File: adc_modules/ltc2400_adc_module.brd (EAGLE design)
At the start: 100 x 80 mm, 0 parts

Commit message: * small modifications on ltc2400_adc_module
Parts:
- added C3: 10u, SquantorRCL:C0805
- added JP1, JP2: (no value), SquantorConnectors:1X10_NORMAL_OCT
- added R2: ferrite, SquantorRCL:R0805
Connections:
- new net GND: C3.1, JP1.2, JP1.3, JP1.6, JP2.1, JP2.2
- new net GND_ADC: JP2.9
- new net N$1: JP1.1, R2.1
- new net N$13: JP2.3
- new net N$14: JP2.4
- new net N$15: JP2.5
- new net N$16: JP2.6
- new net N$17: JP2.7
- new net N$18: JP2.8
- new net V+: JP1.7
- new net V-: JP1.10
- new net VCC_ADC: JP2.10
- new net VCC_VREF: C3.2, R2.2
- new net VIN+: JP1.8
- new net VIN-: JP1.9
- new net VREF_IN: JP1.4
- new net VREF_OUT: JP1.5

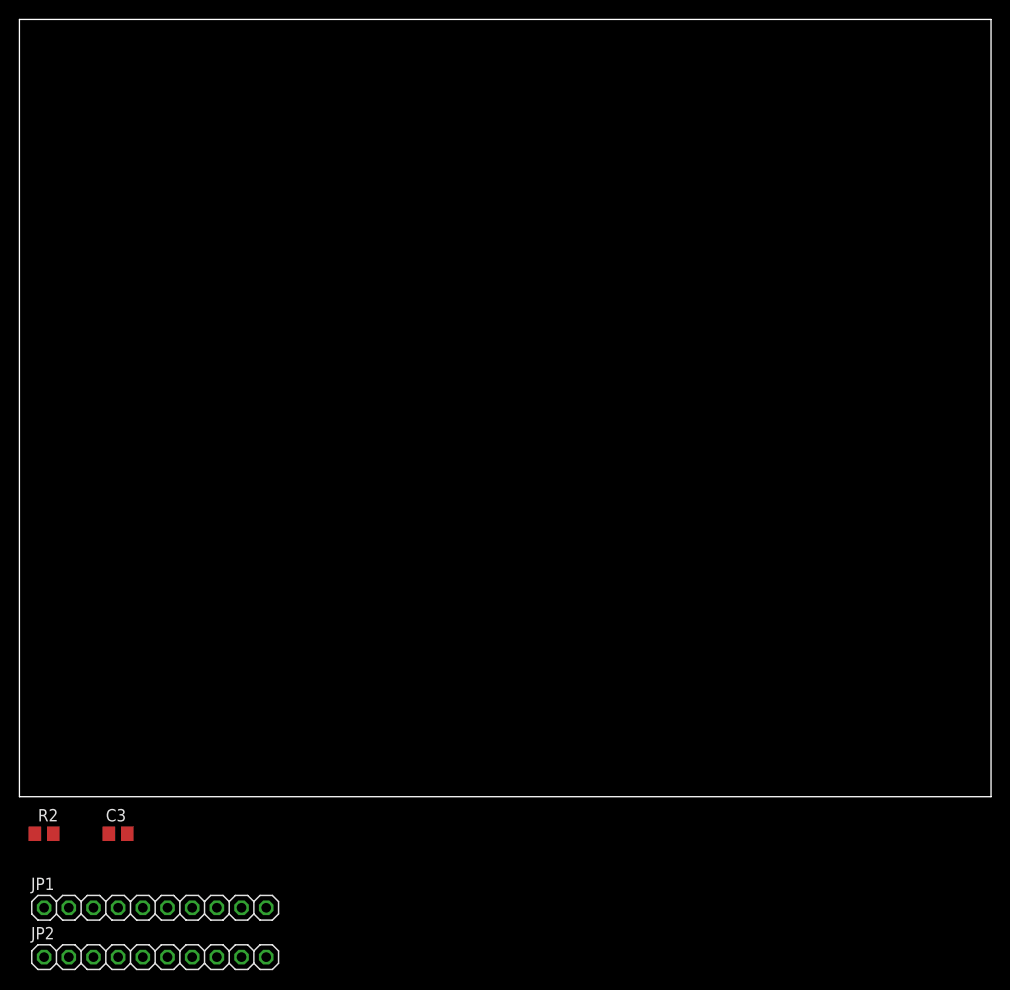
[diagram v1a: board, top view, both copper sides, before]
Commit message: * updated and almost finished MCP3551 ADC module
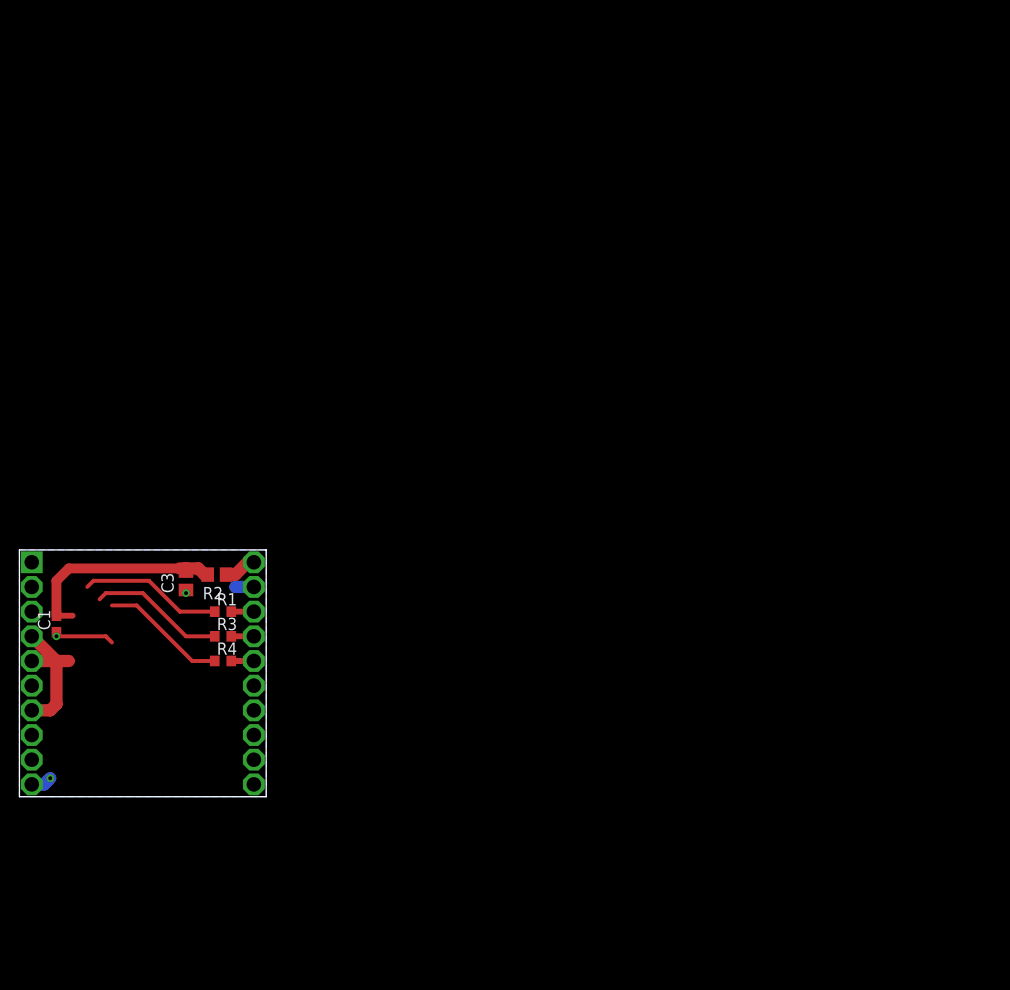
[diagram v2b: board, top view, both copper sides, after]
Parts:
- removed JP1, JP2: (no value), SquantorConnectors:1X10_NORMAL_OCT
- added C1: 100n, SquantorRCL:C0603
- added R1, R3, R4: 100, SquantorRCL:R0603
- added U$1: METROLOGY_MODULE1.5MM, SquantorPCBOutline:METROLOGY_MODULE_1.5MM_HOLE
- moved R2 32.1 mm to (20.3, 22.9), turned to 180 degrees
- moved C3 27.0 mm to (17.1, 22.2), turned to 90 degrees
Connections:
- removed net GND_ADC: JP2.9
- removed net N$13: JP2.3
- removed net N$14: JP2.4
- removed net N$15: JP2.5
- removed net N$16: JP2.6
- removed net N$17: JP2.7
- removed net N$18: JP2.8
- removed net V+: JP1.7
- removed net V-: JP1.10
- removed net VCC_ADC: JP2.10
- removed net VCC_VREF: C3.2, R2.2
- removed net VIN+: JP1.8
- removed net VIN-: JP1.9
- removed net VREF_IN: JP1.4
- removed net VREF_OUT: JP1.5
- new net ADC_CS: R1.1
- new net ADC_SCK: R4.1
- new net ADC_SDO: R3.1
- new net N$2: R1.2, U$1.P$18
- new net N$3: R3.2, U$1.P$17
- new net N$4: R4.2, U$1.P$16
- new net N$5: U$1.P$8
- new net N$6: U$1.P$9
- new net VCC: C1.2, C3.2, R2.2
- new net VREF: U$1.P$4, U$1.P$5, U$1.P$7
- net GND: now also C1.1, U$1.P$10, U$1.P$19, U$1.P$6; no longer JP1.2, JP1.3, JP1.6, JP2.1, JP2.2
- net N$1: now also U$1.P$20; no longer JP1.1
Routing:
- net VCC: track 0.00 -> 21.9 mm
- net VREF: track 0.00 -> 15.1 mm
- net ADC_CS: track 0.00 -> 14.7 mm
- net ADC_SDO: track 0.00 -> 14.0 mm
- net ADC_SCK: track 0.00 -> 12.9 mm
- net GND: track 0.00 -> 10.5 mm, vias 0 -> 3
- net N$1: track 0.00 -> 3.39 mm
- net N$4: track 0.00 -> 2.32 mm
- net N$3: track 0.00 -> 2.32 mm
- net N$2: track 0.00 -> 2.32 mm
- added copper zone on layer 16, net GND
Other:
- board size 100 x 80 mm -> 25.4 x 25.4 mm
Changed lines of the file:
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@@
 <setting verticaltext="up"/>
 </settings>
-<grid distance="2.54" unitdist="mm" unit="mm" style="lines" multiple="1" display="yes" altdistance="0.025" altunitdist="inch" altunit="inch"/>
+<grid distance="0.635" unitdist="mm" unit="mm" style="lines" multiple="1" display="yes" altdistance="0.025" altunitdist="inch" altunit="inch"/>
 <layers>
 <layer number="1" name="Top" color="4" fill="1" visible="yes" active="yes"/>
@@
 <board>
 <plain>
-<wire x1="0" y1="0" x2="100" y2="0" width="0" layer="20"/>
-<wire x1="100" y1="0" x2="100" y2="80" width="0" layer="20"/>
-<wire x1="100" y1="80" x2="0" y2="80" width="0" layer="20"/>
-<wire x1="0" y1="80" x2="0" y2="0" width="0" layer="20"/>
+<wire x1="0" y1="25.4" x2="25.4" y2="25.4" width="0" layer="20"/>
 </plain>
 <attributes>
@@
 </autorouter>
 <elements>
-<element name="JP1" library="SquantorConnectors" package="1X10_NORMAL_OCT" value="" x="13.97" y="-11.43"/>
-<element name="JP2" library="SquantorConnectors" package="1X10_NORMAL_OCT" value="" x="13.97" y="-16.51"/>
-<element name="R2" library="SquantorRCL" package="R0805" value="ferrite" x="2.54" y="-3.81"/>
-<element name="C3" library="SquantorRCL" package="C0805" value="10u" x="10.16" y="-3.81"/>
+<element name="R2" library="SquantorRCL" package="R0805" value="ferrite" x="20.32" y="22.86" rot="R180"/>
+<element name="C3" library="SquantorRCL" package="C0805" value="10u" x="17.145" y="22.225" rot="R90"/>
+<element name="U$1" library="SquantorPCBOutline" package="METROLOGY_MODULE_1.5MM_HOLE" value="METROLOGY_MODULE1.5MM" x="12.7" y="12.7"/>
+<element name="C1" library="SquantorRCL" package="C0603" value="100n" x="3.81" y="17.78" rot="R90"/>
+<element name="R1" library="SquantorRCL" package="R0603" value="100" x="20.955" y="19.05"/>
+<element name="R3" library="SquantorRCL" package="R0603" value="100" x="20.955" y="16.51"/>
+<element name="R4" library="SquantorRCL" package="R0603" value="100" x="20.955" y="13.97"/>
 </elements>
 <signals>
-<signal name="VCC_VREF">
+<signal name="VCC">
 <contactref element="R2" pad="2"/>
 <contactref element="C3" pad="2"/>
-<wire x1="3.49" y1="-3.81" x2="11.11" y2="-3.81" width="0" layer="19" extent="1-1"/>
-</signal>
-<signal name="VREF_IN">
-<contactref element="JP1" pad="4"/>
-</signal>
-<signal name="VREF_OUT">
-<contactref element="JP1" pad="5"/>
-</signal>
-<signal name="V+">
-<contactref element="JP1" pad="7"/>
-</signal>
-<signal name="VIN+">
-<contactref element="JP1" pad="8"/>
-</signal>
-<signal name="VIN-">
-<contactref element="JP1" pad="9"/>
-</signal>
-<signal name="V-">
-<contactref element="JP1" pad="10"/>
+<contactref element="C1" pad="2"/>
+<wire x1="19.37" y1="22.86" x2="19.05" y2="22.86" width="1.27" layer="1"/>
+<wire x1="19.05" y1="22.86" x2="18.415" y2="23.495" width="1.27" layer="1"/>
+<wire x1="18.415" y1="23.495" x2="17.145" y2="23.495" width="1.27" layer="1"/>
+<wire x1="17.145" y1="23.495" x2="16.51" y2="23.495" width="1.27" layer="1"/>
+<wire x1="17.145" y1="23.175" x2="17.145" y2="23.495" width="1.27" layer="1"/>
+<wire x1="16.51" y1="23.495" x2="5.08" y2="23.495" width="1.016" layer="1"/>
+<wire x1="5.08" y1="23.495" x2="3.81" y2="22.225" width="1.016" layer="1"/>
+<wire x1="3.81" y1="22.225" x2="3.81" y2="18.63" width="1.016" layer="1"/>
+<wire x1="3.81" y1="18.63" x2="5.4728" y2="18.63" width="0.6096" layer="1"/>
 </signal>
 <signal name="GND">
-<contactref element="JP2" pad="1"/>
-<contactref element="JP2" pad="2"/>
-<contactref element="JP1" pad="2"/>
-<contactref element="JP1" pad="3"/>
-<contactref element="JP1" pad="6"/>
 <contactref element="C3" pad="1"/>
-<wire x1="5.08" y1="-16.51" x2="2.54" y2="-16.51" width="0" layer="19" extent="1-1"/>
-<wire x1="5.08" y1="-11.43" x2="5.08" y2="-16.51" width="0" layer="19" extent="1-1"/>
-<wire x1="7.62" y1="-11.43" x2="5.08" y2="-11.43" width="0" layer="19" extent="1-1"/>
-<wire x1="15.24" y1="-11.43" x2="7.62" y2="-11.43" width="0" layer="19" extent="1-1"/>
-<wire x1="9.21" y1="-3.81" x2="7.62" y2="-11.43" width="0" layer="19" extent="1-1"/>
-</signal>
-<signal name="N$13">
-<contactref element="JP2" pad="3"/>
-</signal>
-<signal name="N$14">
-<contactref element="JP2" pad="4"/>
-</signal>
-<signal name="N$15">
-<contactref element="JP2" pad="5"/>
-</signal>
-<signal name="N$16">
-<contactref element="JP2" pad="6"/>
-</signal>
-<signal name="N$17">
-<contactref element="JP2" pad="7"/>
-</signal>
-<signal name="N$18">
-<contactref element="JP2" pad="8"/>
-</signal>
-<signal name="GND_ADC">
-<contactref element="JP2" pad="9"/>
-</signal>
-<signal name="VCC_ADC">
-<contactref element="JP2" pad="10"/>
+<contactref element="U$1" pad="P$19"/>
+<contactref element="C1" pad="1"/>
+<polygon width="0.8128" layer="16">
+<vertex x="0" y="25.4"/>
+<vertex x="25.4" y="25.4"/>
+<vertex x="25.4" y="0"/>
+<vertex x="0" y="0"/>
+</polygon>
+<contactref element="U$1" pad="P$6"/>
+<wire x1="24.13" y1="21.59" x2="22.225" y2="21.59" width="1.27" layer="16"/>
+<via x="17.145" y="20.955" extent="1-16" drill="0.4" shape="octagon"/>
+<via x="3.81" y="16.51" extent="1-16" drill="0.4" shape="octagon"/>
+<wire x1="9.525" y1="15.875" x2="8.89" y2="16.51" width="0.4064" layer="1"/>
+<wire x1="8.89" y1="16.51" x2="3.81" y2="16.51" width="0.4064" layer="1"/>
+<wire x1="3.81" y1="16.51" x2="3.81" y2="16.93" width="0.4064" layer="1"/>
+<contactref element="U$1" pad="P$10"/>
+<via x="3.175" y="1.905" extent="1-16" drill="0.4" shape="octagon"/>
+<wire x1="1.27" y1="1.27" x2="2.54" y2="1.27" width="1.27" layer="16"/>
+<wire x1="2.54" y1="1.27" x2="3.175" y2="1.905" width="1.27" layer="16"/>
+<wire x1="17.145" y1="21.275" x2="22.225" y2="21.59" width="0" layer="19" extent="1-16"/>
+<wire x1="17.145" y1="20.955" x2="17.145" y2="21.275" width="0" layer="19" extent="1-1"/>
+<wire x1="9.525" y1="15.875" x2="17.145" y2="20.955" width="0" layer="19" extent="1-1"/>
+<wire x1="1.27" y1="11.43" x2="3.81" y2="16.51" width="0" layer="19" extent="1-1"/>
+<wire x1="3.175" y1="1.905" x2="1.27" y2="11.43" width="0" layer="19" extent="1-1"/>
 </signal>
 <signal name="N$1">
-<contactref element="JP1" pad="1"/>
 <contactref element="R2" pad="1"/>
-<wire x1="1.59" y1="-3.81" x2="2.54" y2="-11.43" width="0" layer="19" extent="1-1"/>
+<contactref element="U$1" pad="P$20"/>
+<wire x1="24.13" y1="24.13" x2="23.495" y2="24.13" width="1.27" layer="1"/>
+<wire x1="23.495" y1="24.13" x2="22.225" y2="22.86" width="1.27" layer="1"/>
+<wire x1="22.225" y1="22.86" x2="21.27" y2="22.86" width="1.27" layer="1"/>
+</signal>
+<signal name="VREF">
+<contactref element="U$1" pad="P$4"/>
+<contactref element="U$1" pad="P$5"/>
+<wire x1="1.27" y1="13.97" x2="3.81" y2="13.97" width="1.27" layer="1"/>
+<wire x1="3.81" y1="13.97" x2="5.08" y2="13.97" width="1.27" layer="1"/>
+<wire x1="1.27" y1="16.51" x2="3.81" y2="13.97" width="1.27" layer="1"/>
+<wire x1="5.08" y1="13.97" x2="5.5372" y2="13.97" width="0.4064" layer="1"/>
+<contactref element="U$1" pad="P$7"/>
+<wire x1="1.27" y1="8.89" x2="3.175" y2="8.89" width="1.27" layer="1"/>
+<wire x1="3.175" y1="8.89" x2="3.81" y2="9.525" width="1.27" layer="1"/>
+<wire x1="3.81" y1="9.525" x2="3.81" y2="13.97" width="1.27" layer="1"/>
+</signal>
+<signal name="N$2">
+<contactref element="U$1" pad="P$18"/>
+<contactref element="R1" pad="2"/>
+<wire x1="24.13" y1="19.05" x2="21.805" y2="19.05" width="0.6096" layer="1"/>
+</signal>
+<signal name="N$3">
+<contactref element="U$1" pad="P$17"/>
+<contactref element="R3" pad="2"/>
+<wire x1="24.13" y1="16.51" x2="21.805" y2="16.51" width="0.6096" layer="1"/>
+</signal>
+<signal name="N$4">
+<contactref element="U$1" pad="P$16"/>
+<contactref element="R4" pad="2"/>
+<wire x1="24.13" y1="13.97" x2="21.805" y2="13.97" width="0.6096" layer="1"/>
+</signal>
+<signal name="ADC_CS">
+<contactref element="R1" pad="1"/>
+<wire x1="20.105" y1="19.05" x2="16.51" y2="19.05" width="0.4064" layer="1"/>
+<wire x1="16.51" y1="19.05" x2="13.335" y2="22.225" width="0.4064" layer="1"/>
+<wire x1="13.335" y1="22.225" x2="7.62" y2="22.225" width="0.4064" layer="1"/>
+<wire x1="7.62" y1="22.225" x2="6.985" y2="21.59" width="0.4064" layer="1"/>
+</signal>
+<signal name="ADC_SDO">
+<contactref element="R3" pad="1"/>
+<wire x1="20.105" y1="16.51" x2="17.145" y2="16.51" width="0.4064" layer="1"/>
+<wire x1="17.145" y1="16.51" x2="12.7" y2="20.955" width="0.4064" layer="1"/>
+<wire x1="12.7" y1="20.955" x2="8.89" y2="20.955" width="0.4064" layer="1"/>
+<wire x1="8.89" y1="20.955" x2="8.255" y2="20.32" width="0.4064" layer="1"/>
+</signal>
+<signal name="ADC_SCK">
+<contactref element="R4" pad="1"/>
+<wire x1="20.105" y1="13.97" x2="17.78" y2="13.97" width="0.4064" layer="1"/>
+<wire x1="17.78" y1="13.97" x2="12.065" y2="19.685" width="0.4064" layer="1"/>
+<wire x1="12.065" y1="19.685" x2="9.525" y2="19.685" width="0.4064" layer="1"/>
+</signal>
+<signal name="N$5">
+<contactref element="U$1" pad="P$8"/>
+</signal>
+<signal name="N$6">
+<contactref element="U$1" pad="P$9"/>
 </signal>
 </signals>
